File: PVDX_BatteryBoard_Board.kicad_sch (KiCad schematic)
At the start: 6 parts

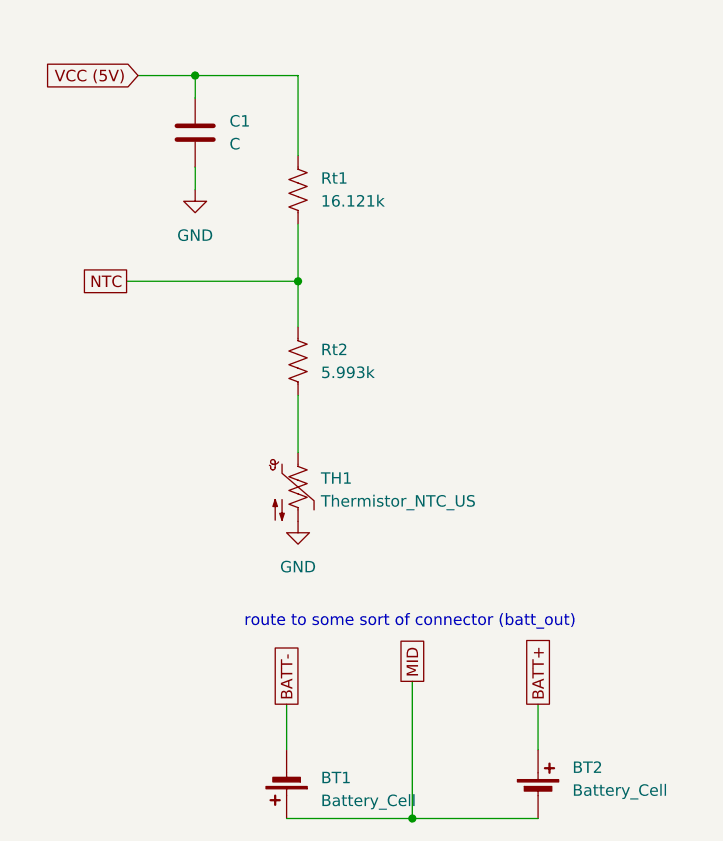
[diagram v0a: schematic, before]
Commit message: added heater schematic
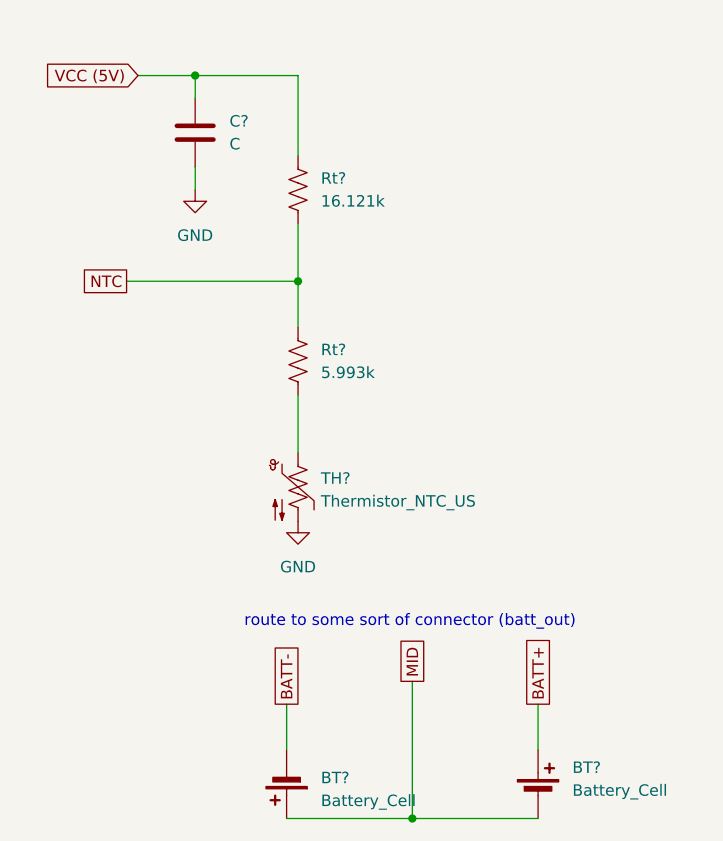
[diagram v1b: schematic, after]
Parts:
- renumbered BT2 to BT?, BT1 to BT?, C1 to C?, Rt2 to Rt?, Rt1 to Rt?, TH1 to TH?
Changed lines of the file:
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@@
 		(dnp no)
 		(fields_autoplaced yes)
-		(property "Reference" "TH1"
+		(property "Reference" "TH?"
 			(at 92.71 95.5674 0)
 			(effects
@@
 		)
 		(instances
+			(project "PVDX_BatteryBoard"
+				(path "/c318761a-e6d3-4e59-aaa2-0d170bce7cde/0a3f63ce-136a-4115-ab54-eabf7e58dfd1"
+					(reference "TH?")
+					(unit 1)
+				)
+			)
 			(project "PVDX_BatteryBoard_Board"
 				(path "/e7c095aa-cf75-4f7e-8bb1-3b099b992029"
@@
 		(dnp no)
 		(fields_autoplaced yes)
-		(property "Reference" "Rt2"
+		(property "Reference" "Rt?"
 			(at 92.71 81.2799 0)
 			(effects
@@
 		)
 		(instances
+			(project "PVDX_BatteryBoard"
+				(path "/c318761a-e6d3-4e59-aaa2-0d170bce7cde/0a3f63ce-136a-4115-ab54-eabf7e58dfd1"
+					(reference "Rt?")
+					(unit 1)
+				)
+			)
 			(project "PVDX_BatteryBoard_Board"
 				(path "/e7c095aa-cf75-4f7e-8bb1-3b099b992029"
@@
 		(dnp no)
 		(fields_autoplaced yes)
-		(property "Reference" "BT2"
+		(property "Reference" "BT?"
 			(at 120.65 127.6984 0)
 			(effects
@@
 		)
 		(instances
+			(project "PVDX_BatteryBoard"
+				(path "/c318761a-e6d3-4e59-aaa2-0d170bce7cde/0a3f63ce-136a-4115-ab54-eabf7e58dfd1"
+					(reference "BT?")
+					(unit 1)
+				)
+			)
 			(project "PVDX_BatteryBoard_Board"
 				(path "/e7c095aa-cf75-4f7e-8bb1-3b099b992029"
@@
 		(dnp no)
 		(fields_autoplaced yes)
-		(property "Reference" "Rt1"
+		(property "Reference" "Rt?"
 			(at 92.71 62.2299 0)
 			(effects
@@
 		)
 		(instances
+			(project "PVDX_BatteryBoard"
+				(path "/c318761a-e6d3-4e59-aaa2-0d170bce7cde/0a3f63ce-136a-4115-ab54-eabf7e58dfd1"
+					(reference "Rt?")
+					(unit 1)
+				)
+			)
 			(project "PVDX_BatteryBoard_Board"
 				(path "/e7c095aa-cf75-4f7e-8bb1-3b099b992029"
@@
 		(dnp no)
 		(fields_autoplaced yes)
-		(property "Reference" "C1"
+		(property "Reference" "C?"
 			(at 82.55 55.8799 0)
 			(effects
@@
 		)
 		(instances
+			(project "PVDX_BatteryBoard"
+				(path "/c318761a-e6d3-4e59-aaa2-0d170bce7cde/0a3f63ce-136a-4115-ab54-eabf7e58dfd1"
+					(reference "C?")
+					(unit 1)
+				)
+			)
 			(project "PVDX_BatteryBoard_Board"
 				(path "/e7c095aa-cf75-4f7e-8bb1-3b099b992029"
@@
 		(dnp no)
 		(fields_autoplaced yes)
-		(property "Reference" "#PWR02"
+		(property "Reference" "#PWR?"
 			(at 78.74 69.85 0)
 			(effects
@@
 		)
 		(instances
+			(project "PVDX_BatteryBoard"
+				(path "/c318761a-e6d3-4e59-aaa2-0d170bce7cde/0a3f63ce-136a-4115-ab54-eabf7e58dfd1"
+					(reference "#PWR?")
+					(unit 1)
+				)
+			)
 			(project "PVDX_BatteryBoard_Board"
 				(path "/e7c095aa-cf75-4f7e-8bb1-3b099b992029"
@@
 		(dnp no)
 		(fields_autoplaced yes)
-		(property "Reference" "BT1"
+		(property "Reference" "BT?"
 			(at 92.71 128.8414 0)
 			(effects
@@
 		)
 		(instances
+			(project "PVDX_BatteryBoard"
+				(path "/c318761a-e6d3-4e59-aaa2-0d170bce7cde/0a3f63ce-136a-4115-ab54-eabf7e58dfd1"
+					(reference "BT?")
+					(unit 1)
+				)
+			)
 			(project "PVDX_BatteryBoard_Board"
 				(path "/e7c095aa-cf75-4f7e-8bb1-3b099b992029"
@@
 		(dnp no)
 		(fields_autoplaced yes)
-		(property "Reference" "#PWR01"
+		(property "Reference" "#PWR?"
 			(at 90.17 106.68 0)
 			(effects
@@
 		)
 		(instances
-			(project "PVDX_BatteryBoard_Board"
-				(path "/e7c095aa-cf75-4f7e-8bb1-3b099b992029"
+			(project "PVDX_BatteryBoard"
+				(path "/c318761a-e6d3-4e59-aaa2-0d170bce7cde/0a3f63ce-136a-4115-ab54-eabf7e58dfd1"
+					(reference "#PWR?")
+					(unit 1)
+				)
+			)
+			(project "PVDX_BatteryBoard_Board"
+				(path "/e7c095aa-cf75-4f7e-8bb1-3b099b992029"

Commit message: added solar connectors schematic
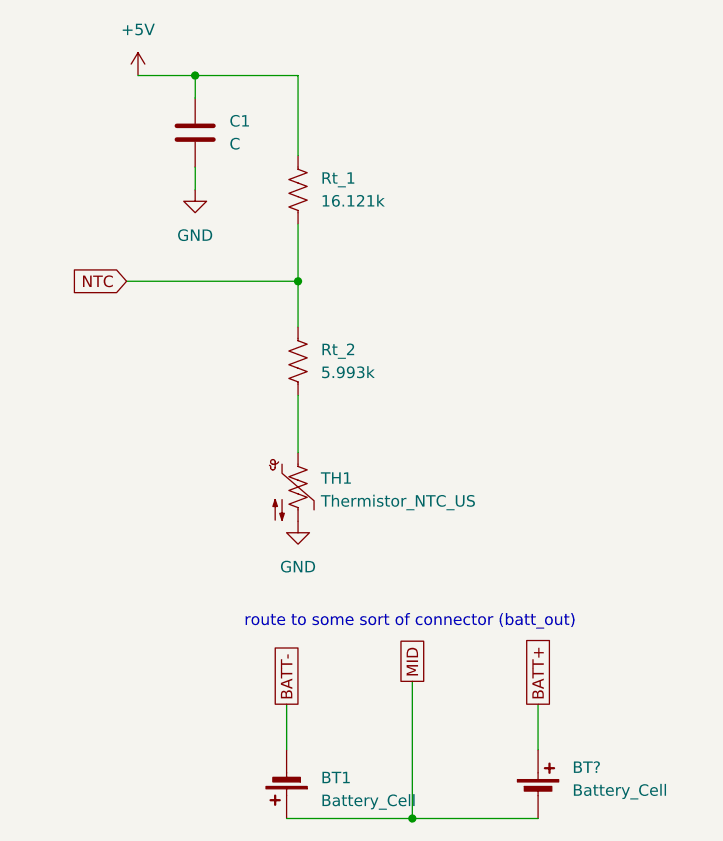
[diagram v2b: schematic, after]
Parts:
- gave numbers to parts that had none: 5
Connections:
- net VCC (5V) renamed +5V
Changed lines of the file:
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@@
 		)
 	)
-	(global_label "VCC (5V)"
-		(shape input)
-		(at 72.39 50.8 180)
+	(global_label "BATT-"
+		(shape passive)
+		(at 88.9 120.65 90)
 		(fields_autoplaced yes)
 		(effects
@@
 				(size 1.27 1.27)
 			)
-			(justify right)
+			(justify left)
 		)
 		(property "Intersheetrefs" "${INTERSHEET_REFS}"
-			(at 60.8171 50.8 0)
-			(effects
-				(font
-					(size 1.27 1.27)
-				)
-				(justify right)
-				(hide yes)
-			)
-		)
-	)
-	(global_label "BATT-"
-		(shape passive)
-		(at 88.9 120.65 90)
+			(at 88.9 112.9099 90)
+			(effects
+				(font
+					(size 1.27 1.27)
+				)
+				(justify left)
+				(hide yes)
+			)
+		)
+	)
+	(global_label "NTC"
+		(shape input)
+		(at 71.12 73.66 180)
 		(fields_autoplaced yes)
 		(effects
@@
 				(size 1.27 1.27)
 			)
-			(justify left)
+			(justify right)
 		)
 		(property "Intersheetrefs" "${INTERSHEET_REFS}"
-			(at 88.9 112.9099 90)
-			(effects
-				(font
-					(size 1.27 1.27)
-				)
-				(justify left)
-				(hide yes)
-			)
-		)
-	)
-	(global_label "NTC"
-		(shape passive)
-		(at 71.12 73.66 180)
-		(fields_autoplaced yes)
-		(effects
-			(font
-				(size 1.27 1.27)
-			)
-			(justify right)
-		)
-		(property "Intersheetrefs" "${INTERSHEET_REFS}"
-			(at 65.678 73.66 0)
+			(at 64.5667 73.66 0)
 			(effects
 				(font
@@
 		(dnp no)
 		(fields_autoplaced yes)
-		(property "Reference" "TH?"
+		(property "Reference" "TH1"
 			(at 92.71 95.5674 0)
 			(effects
@@
 			(project "PVDX_BatteryBoard"
 				(path "/c318761a-e6d3-4e59-aaa2-0d170bce7cde/0a3f63ce-136a-4115-ab54-eabf7e58dfd1"
-					(reference "TH?")
+					(reference "TH1")
 					(unit 1)
 				)
@@
 		(dnp no)
 		(fields_autoplaced yes)
-		(property "Reference" "Rt?"
+		(property "Reference" "Rt_2"
 			(at 92.71 81.2799 0)
 			(effects
@@
 			(project "PVDX_BatteryBoard"
 				(path "/c318761a-e6d3-4e59-aaa2-0d170bce7cde/0a3f63ce-136a-4115-ab54-eabf7e58dfd1"
-					(reference "Rt?")
+					(reference "Rt_2")
 					(unit 1)
 				)
@@
 		(dnp no)
 		(fields_autoplaced yes)
-		(property "Reference" "Rt?"
+		(property "Reference" "Rt_1"
 			(at 92.71 62.2299 0)
 			(effects
@@
 			(project "PVDX_BatteryBoard"
 				(path "/c318761a-e6d3-4e59-aaa2-0d170bce7cde/0a3f63ce-136a-4115-ab54-eabf7e58dfd1"
-					(reference "Rt?")
+					(reference "Rt_1")
 					(unit 1)
 				)
@@
 		(dnp no)
 		(fields_autoplaced yes)
-		(property "Reference" "C?"
+		(property "Reference" "C1"
 			(at 82.55 55.8799 0)
 			(effects
@@
 			(project "PVDX_BatteryBoard"
 				(path "/c318761a-e6d3-4e59-aaa2-0d170bce7cde/0a3f63ce-136a-4115-ab54-eabf7e58dfd1"
-					(reference "C?")
+					(reference "C1")
 					(unit 1)
 				)
@@
 	)
 	(symbol
+		(lib_id "power:+5V")
+		(at 72.39 50.8 0)
+		(unit 1)
+		(exclude_from_sim no)
+		(in_bom yes)
+		(on_board yes)
+		(dnp no)
+		(fields_autoplaced yes)
+		(property "Reference" "#PWR04"
+			(at 72.39 54.61 0)
+			(effects
+				(font
+					(size 1.27 1.27)
+				)
+				(hide yes)
+			)
+		)
+		(property "Value" "+5V"
+			(at 72.39 45.72 0)
+			(effects
+				(font
+					(size 1.27 1.27)
+				)
+			)
+		)
+		(property "Footprint" ""
+			(at 72.39 50.8 0)
+			(effects
+				(font
+					(size 1.27 1.27)
+				)
+				(hide yes)
+			)
+		)
+		(property "Datasheet" ""
+			(at 72.39 50.8 0)
+			(effects
+				(font
+					(size 1.27 1.27)
+				)
+				(hide yes)
+			)
+		)
+		(property "Description" "Power symbol creates a global label with name \"+5V\""
+			(at 72.39 50.8 0)
+			(effects
+				(font
+					(size 1.27 1.27)
+				)
+				(hide yes)
+			)
+		)
+		(pin "1"
+		)
+		(instances
+			(project ""
+				(path "/c318761a-e6d3-4e59-aaa2-0d170bce7cde/0a3f63ce-136a-4115-ab54-eabf7e58dfd1"
+					(reference "#PWR04")
+					(unit 1)
+				)
+			)
+		)
+	)
+	(symbol
 		(lib_id "Device:Battery_Cell")
 		(at 88.9 128.27 180)
@@
 		(dnp no)
 		(fields_autoplaced yes)
-		(property "Reference" "BT?"
+		(property "Reference" "BT1"
 			(at 92.71 128.8414 0)
 			(effects
@@
 			(project "PVDX_BatteryBoard"
 				(path "/c318761a-e6d3-4e59-aaa2-0d170bce7cde/0a3f63ce-136a-4115-ab54-eabf7e58dfd1"
-					(reference "BT?")
-					(unit 1)
-				)
+					(reference "BT1")
+					(unit 1)
+				)
